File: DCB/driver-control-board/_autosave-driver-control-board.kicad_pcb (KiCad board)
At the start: 2 copper layers, 92.7 x 59.2 mm, 33 parts, among them J1 Conn_01x05, J2 Conn_01x14, J3 Conn_01x08, J4 Conn_01x23, U1 STM32F413CGUx, U2 LD1117S33TR_SOT223, U3 R-78B5.0-2.0, U4 MCP2551-I-SN, Y1 Crystal

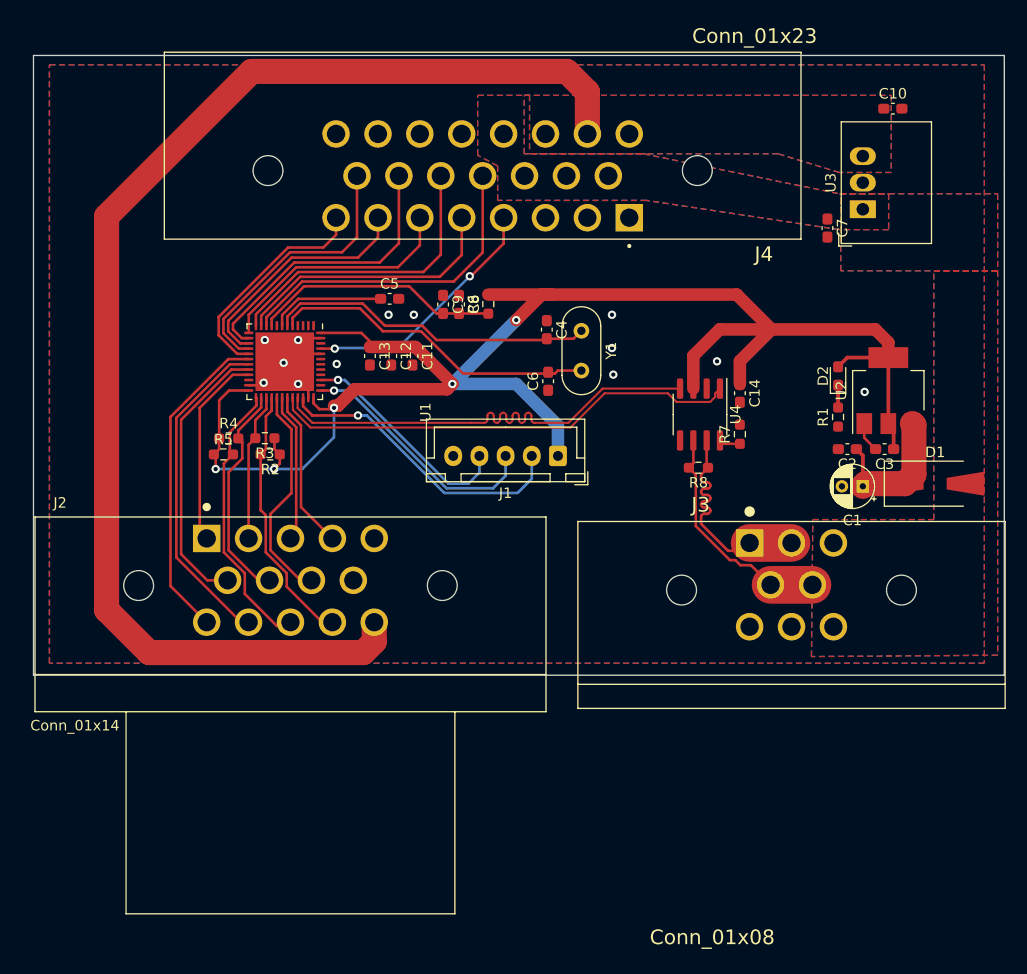
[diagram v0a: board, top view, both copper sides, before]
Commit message: DCB Layout Rev 1 Complete
Complete the layout first draft
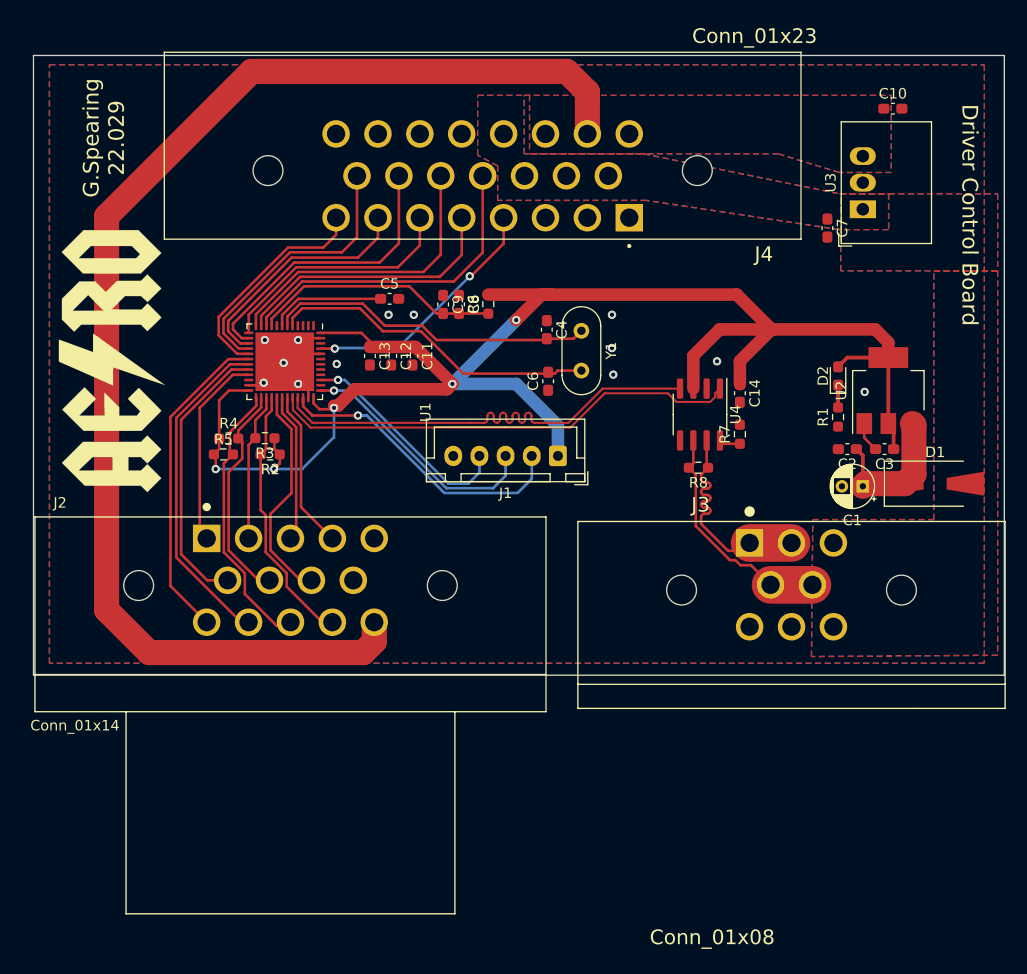
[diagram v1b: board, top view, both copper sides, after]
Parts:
- added G***: LOGO, AERO_Footprints:AERO_Logo_25x10mm, F.Cu at (103.0, 134.4)
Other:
- board text added: "Driver Control Board"
- board text added: "G.Spearing 22.029"
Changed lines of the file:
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@@
     )
+  )
+  (footprint "AERO_Footprints:AERO_Logo_25x10mm" (layer "F.Cu")
+    (at 102.997 134.366 90)
+    (attr through_hole)
+    (fp_text reference "G***" (at 0 0 90) (layer "F.SilkS") hide
+      (effects (font (size 1.524 1.524) (thickness 0.3)))
+    )
+    (fp_text value "LOGO" (at 0.75 0 90) (layer "F.SilkS") hide
+      (effects (font (size 1.524 1.524) (thickness 0.3)))
+    )
+    (fp_poly (pts
+        (xy 1.48555 -3.437156)
+        (xy 0.88742 -1.805963)
+        (xy 1.792647 -1.805963)
+        (xy 2.13411 -1.805266)
+        (xy 2.374206 -1.801911)
+        (xy 2.528081 -1.794001)
+        (xy 2.610878 -1.779642)
+        (xy 2.637744 -1.756938)
+        (xy 2.623822 -1.723993)
+        (xy 2.607124 -1.704014)
+        (xy 2.560496 -1.642703)
+        (xy 2.452739 -1.496064)
+        (xy 2.2906 -1.273472)
+        (xy 2.080823 -0.984301)
+        (xy 1.830152 -0.637926)
+        (xy 1.545334 -0.243722)
+        (xy 1.233113 0.188937)
+        (xy 0.900234 0.650674)
+        (xy 0.553443 1.132116)
+        (xy 0.199483 1.623887)
+        (xy -0.154899 2.116613)
+        (xy -0.502959 2.600919)
+        (xy -0.837952 3.06743)
+        (xy -1.153132 3.506771)
+        (xy -1.441755 3.909568)
+        (xy -1.697076 4.266444)
+        (xy -1.912349 4.568027)
+        (xy -2.08083 4.80494)
+        (xy -2.195773 4.967808)
+        (xy -2.250434 5.047258)
+        (xy -2.251631 5.049138)
+        (xy -2.247031 5.018182)
+        (xy -2.207458 4.887527)
+        (xy -2.136353 4.667475)
+        (xy -2.037157 4.368325)
+        (xy -1.913312 4.000379)
+        (xy -1.768257 3.573937)
+        (xy -1.605433 3.099301)
+        (xy -1.450599 2.651135)
+        (xy -1.272624 2.137289)
+        (xy -1.106931 1.658286)
+        (xy -0.957313 1.225136)
+        (xy -0.827562 0.84885)
+        (xy -0.721473 0.540437)
+        (xy -0.642839 0.310908)
+        (xy -0.595452 0.171273)
+        (xy -0.582569 0.131524)
+        (xy -0.637453 0.126278)
+        (xy -0.788619 0.121831)
+        (xy -1.015833 0.118534)
+        (xy -1.298863 0.116739)
+        (xy -1.448313 0.116514)
+        (xy -2.314057 0.116514)
+        (xy -1.663387 -1.354472)
+        (xy -1.457671 -1.81999)
+        (xy -1.235644 -2.323191)
+        (xy -1.011221 -2.832488)
+        (xy -0.798318 -3.316289)
+        (xy -0.610849 -3.743005)
+        (xy -0.521442 -3.946904)
+        (xy -0.030166 -5.068348)
+        (xy 2.083681 -5.068348)
+        (xy 1.48555 -3.437156)
+      ) (layer "F.SilkS") (width 0.01) (fill solid))
+    (fp_poly (pts
+        (xy -2.477659 -2.622121)
+        (xy -3.029276 -2.068201)
+        (xy -3.580892 -1.514282)
+        (xy -5.184862 -3.115182)
+        (xy -5.184862 -0.69421)
+        (xy -4.078692 -0.711211)
+        (xy -2.972522 -0.728211)
+        (xy -4.396646 0.699083)
+        (xy -5.184862 0.699083)
+        (xy -5.184862 2.382603)
+        (xy -4.977207 2.540989)
+        (xy -4.769551 2.699376)
+        (xy -4.175481 2.107328)
+        (xy -3.581411 1.515279)
+        (xy -2.530301 2.566389)
+        (xy -3.611941 3.642598)
+        (xy -3.902517 3.930701)
+        (xy -4.165689 4.189694)
+        (xy -4.390326 4.40878)
+        (xy -4.565301 4.577165)
+        (xy -4.679482 4.684053)
+        (xy -4.72142 4.718807)
+        (xy -4.768729 4.679379)
+        (xy -4.886204 4.568805)
+        (xy -5.061953 4.398654)
+        (xy -5.284083 4.180497)
+        (xy -5.540701 3.925902)
+        (xy -5.695272 3.77149)
+        (xy -6.641284 2.824173)
+        (xy -6.641284 -2.704844)
+        (xy -5.623333 -3.72851)
+        (xy -4.605381 -4.752177)
+        (xy -2.477659 -2.622121)
+      ) (layer "F.SilkS") (width 0.01) (fill solid))
+    (fp_poly (pts
+        (xy 6.802244 -3.946175)
+        (xy 7.631651 -3.115285)
+        (xy 7.631651 -1.604369)
+        (xy 7.123086 -1.093437)
+        (xy 6.614521 -0.582504)
+        (xy 7.152215 -0.042566)
+        (xy 7.689908 0.497373)
+        (xy 7.689908 2.763538)
+        (xy 7.994602 3.072064)
+        (xy 8.299295 3.38059)
+        (xy 6.960436 4.719449)
+        (xy 6.307049 4.063738)
+        (xy 5.653662 3.408028)
+        (xy 6.228442 2.767202)
+        (xy 6.233486 1.250536)
+        (xy 5.592661 0.611697)
+        (xy 4.951835 -0.027141)
+        (xy 4.951835 2.829839)
+        (xy 5.243762 3.117377)
+        (xy 5.53569 3.404915)
+        (xy 4.880607 4.061861)
+        (xy 4.656022 4.284832)
+        (xy 4.45981 4.475378)
+        (xy 4.306705 4.619528)
+        (xy 4.21144 4.703309)
+        (xy 4.187859 4.718807)
+        (xy 4.136831 4.678799)
+        (xy 4.020352 4.568311)
+        (xy 3.852889 4.401644)
+        (xy 3.648913 4.193102)
+        (xy 3.512625 4.05132)
+        (xy 2.875057 3.383832)
+        (xy 3.495413 2.771182)
+        (xy 3.495413 -0.787039)
+        (xy 4.835321 -0.787039)
+        (xy 6.3203 -2.272018)
+        (xy 5.577811 -3.014508)
+        (xy 4.835321 -3.756998)
+        (xy 4.835321 -0.787039)
+        (xy 3.495413 -0.787039)
+        (xy 3.495413 -2.938594)
+        (xy 3.161895 -3.275628)
+        (xy 2.828378 -3.612662)
+        (xy 3.98841 -4.777064)
+        (xy 5.972837 -4.777064)
+        (xy 6.802244 -3.946175)
+      ) (layer "F.SilkS") (width 0.01) (fill solid))
+    (fp_poly (pts
+        (xy 12.525229 -2.710159)
+        (xy 12.525229 2.535324)
+        (xy 10.339393 4.71889)
+        (xy 9.364192 3.742421)
+        (xy 8.388991 2.765953)
+        (xy 8.388991 2.2956)
+        (xy 9.845413 2.2956)
+        (xy 10.032432 2.488555)
+        (xy 10.219452 2.68151)
+        (xy 11.01055 1.896474)
+        (xy 11.01055 -2.012048)
+        (xy 10.427982 -2.592431)
+        (xy 9.845413 -3.172814)
+        (xy 9.845413 2.2956)
+        (xy 8.388991 2.2956)
+        (xy 8.388991 -2.76845)
+        (xy 9.408495 -3.786706)
+        (xy 10.427999 -4.804961)
+        (xy 12.525229 -2.710159)
+      ) (layer "F.SilkS") (width 0.01) (fill solid))
+    (fp_poly (pts
+        (xy -8.694247 -3.771558)
+        (xy -7.689908 -2.765987)
+        (xy -7.689908 2.763538)
+        (xy -7.385215 3.072064)
+        (xy -7.080521 3.38059)
+        (xy -7.749951 4.050019)
+        (xy -8.41938 4.719449)
+        (xy -9.755082 3.379947)
+        (xy -9.450706 3.071743)
+        (xy -9.14633 2.763538)
+        (xy -9.14633 1.572936)
+        (xy -10.427982 1.572936)
+        (xy -10.427982 2.763538)
+        (xy -10.123288 3.072064)
+        (xy -9.818595 3.38059)
+        (xy -11.157454 4.719449)
+        (xy -11.825305 4.049698)
+        (xy -12.493155 3.379947)
+        (xy -12.18878 3.071743)
+        (xy -11.884404 2.763538)
+        (xy -11.884404 0.058257)
+        (xy -10.427982 0.058257)
+        (xy -9.14633 0.058257)
+        (xy -9.14633 -1.838329)
+        (xy -9.784204 -2.506665)
+        (xy -10.422078 -3.175)
+        (xy -10.42503 -1.558371)
+        (xy -10.427982 0.058257)
+        (xy -11.884404 0.058257)
+        (xy -11.884404 -2.593581)
+        (xy -10.791495 -3.685355)
+        (xy -9.698586 -4.777128)
+        (xy -8.694247 -3.771558)
+      ) (layer "F.SilkS") (width 0.01) (fill solid))
   )
   (footprint "Diode_SMD:D_SMA-SMB_Universal_Handsoldering" (layer "F.Cu")
@@
   (gr_line (start 188.214 164.338) (end 188.214 116.586) (layer "Edge.Cuts") (width 0.1))
   (gr_line (start 188.214 116.586) (end 188.214 105.156) (layer "Edge.Cuts") (width 0.1))
+  (gr_text "G.Spearing\n22.029" (at 102.235 113.03 90) (layer "F.SilkS")
+    (effects (font (size 1.5 1.5) (thickness 0.3)))
+  )
+  (gr_text "Driver Control Board" (at 184.912 120.396 270) (layer "F.SilkS")
+    (effects (font (size 1.5 1.5) (thickness 0.3)))
+  )
   (segment (start 179.58352 145.17648) (end 178.71 146.05) (width 2.4) (layer "F.Cu") (net 1))
   (segment (start 179.58352 140.45352) (end 179.58352 145.17648) (width 2.4) (layer "F.Cu") (net 1))
